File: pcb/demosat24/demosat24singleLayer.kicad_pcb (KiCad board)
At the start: 2 copper layers, 68.6 x 53.3 mm, 28 parts, among them J1 Power, J10 Conn_01x03, J11 Conn_01x02, J12 Conn_01x02, J13 Conn_01x03, J2 Digital/PWM, J3 Analog, J4 Digital/PWM, J5 Conn_01x04, J6 Conn_01x04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

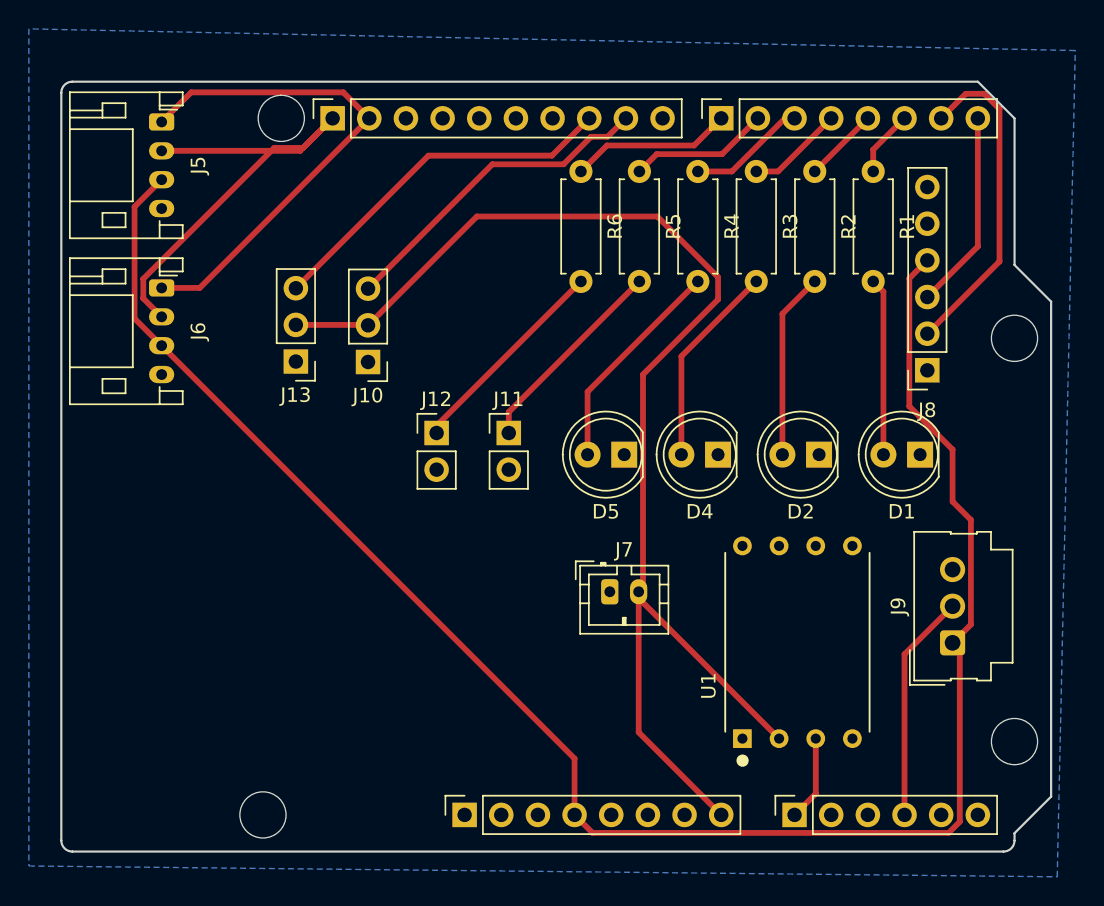
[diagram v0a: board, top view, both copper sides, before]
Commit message: PCB Ordered! switched to dual layer board with ground plane added headers for a second servo cleaned up repo
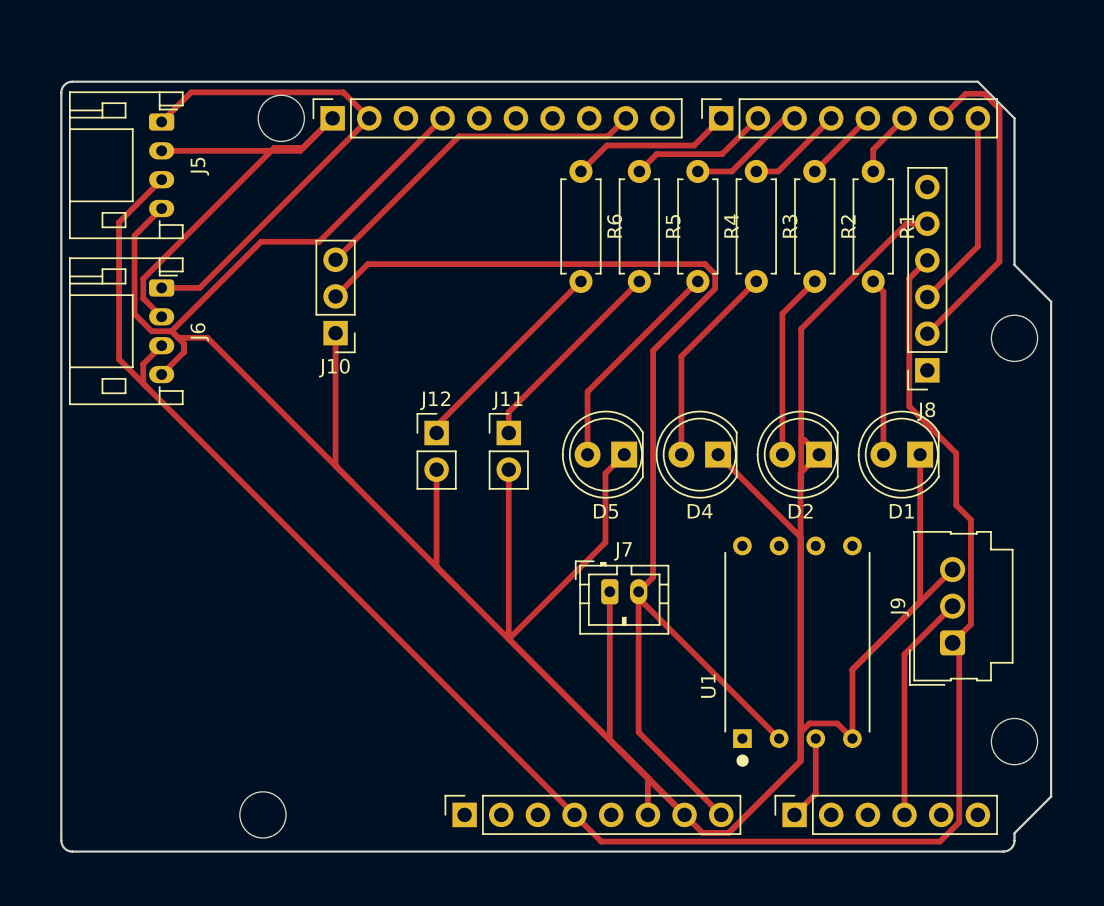
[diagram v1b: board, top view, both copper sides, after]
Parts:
- removed J13: Conn_01x03, Connector_PinHeader_2.54mm:PinHeader_1x03_P2.54mm_Vertical
- moved J10 3.01 mm to (119.0, 64.1)
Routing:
- net GND: track 0.00 -> 300.3 mm
- net /*10: track 25.2 -> 0.00 mm
- net VCC: track 89.5 -> 83.3 mm
- net +3V3: track 126.2 -> 131.1 mm
- net /*9: track 22.8 -> 24.2 mm
- removed copper zone on B.Cu, net GND
